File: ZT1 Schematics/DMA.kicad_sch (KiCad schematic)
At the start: 11 parts, among them U106 74LS32, U109 74LS368, U112 74LS368, U115 74LS32, U128 74LS74, U131 74LS08, U132 74LS10

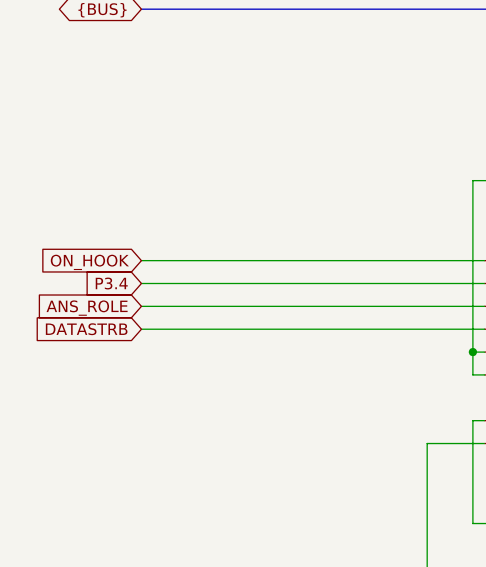
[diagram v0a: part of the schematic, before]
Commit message: Minor touchups
Fixed some of the text
Added some explanations
Simplified the video circuit
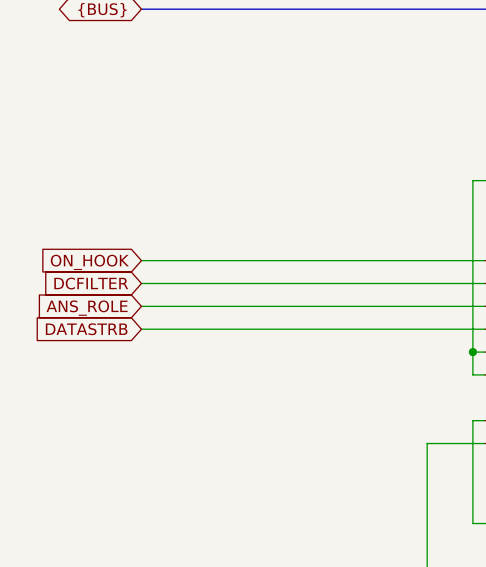
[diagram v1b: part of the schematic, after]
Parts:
- C115, C139: footprint ZX1:C_350mil -> ZT1:C_350mil
- R153: footprint ZX1:R_450mil -> ZT1:R_450mil
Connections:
- net P3.4 renamed DCFILTER
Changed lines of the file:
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@@
 		)
 	)
-	(global_label "P3.4"
+	(global_label "DCFILTER"
 		(shape input)
 		(at 43.18 93.98 180)
@@
 		)
 		(property "Intersheetrefs" "${INTERSHEET_REFS}"
-			(at 35.901 93.98 0)
+			(at 31.5467 93.98 0)
 			(effects
 				(font
@@
 		)
 		(instances
-			(project "ZX1"
+			(project "ZT1"
 				(path "/f4096561-d684-4672-ab54-4b1ef20fc4c8/ca6d4eac-07c0-4b7b-97f3-ce02b2439cee"
 					(reference "#PWR094")
@@
 	)
 	(symbol
-		(lib_name "74LS10_2")
 		(lib_id "74xx:74LS10")
 		(at 170.18 45.72 0)
@@
 		)
 		(instances
-			(project "ZX1"
+			(project "ZT1"
 				(path "/f4096561-d684-4672-ab54-4b1ef20fc4c8/ca6d4eac-07c0-4b7b-97f3-ce02b2439cee"
 					(reference "U132")
@@
 		)
 		(instances
-			(project "ZX1"
+			(project "ZT1"
 				(path "/f4096561-d684-4672-ab54-4b1ef20fc4c8/ca6d4eac-07c0-4b7b-97f3-ce02b2439cee"
 					(reference "U115")
@@
 		)
 		(instances
-			(project "ZX1"
+			(project "ZT1"
 				(path "/f4096561-d684-4672-ab54-4b1ef20fc4c8/ca6d4eac-07c0-4b7b-97f3-ce02b2439cee"
 					(reference "U112")
@@
 		)
 		(instances
-			(project "ZX1"
+			(project "ZT1"
 				(path "/f4096561-d684-4672-ab54-4b1ef20fc4c8/ca6d4eac-07c0-4b7b-97f3-ce02b2439cee"
 					(reference "#PWR093")
@@
 			)
 		)
-		(property "Footprint" "ZX1:C_350mil"
+		(property "Footprint" "ZT1:C_350mil"
 			(at 107.95 81.5848 0)
 			(effects
@@
 			)
 		)
-		(property "Datasheet" ""
+		(property "Datasheet" "~"
 			(at 104.14 82.55 0)
 			(effects
@@
 			)
 		)
-		(property "Description" ""
+		(property "Description" "Unpolarized capacitor"
 			(at 104.14 82.55 0)
 			(effects
@@
 		)
 		(instances
-			(project "ZX1"
+			(project "ZT1"
 				(path "/f4096561-d684-4672-ab54-4b1ef20fc4c8/ca6d4eac-07c0-4b7b-97f3-ce02b2439cee"
 					(reference "#PWR092")
@@
 		)
 		(instances
-			(project "ZX1"
+			(project "ZT1"
 				(path "/f4096561-d684-4672-ab54-4b1ef20fc4c8/ca6d4eac-07c0-4b7b-97f3-ce02b2439cee"
 					(reference "#PWR090")
@@
 			)
 		)
-		(property "Footprint" "ZX1:C_350mil"
+		(property "Footprint" "ZT1:C_350mil"
 			(at 262.89 29.5148 0)
 			(effects
@@
 			)
 		)
-		(property "Datasheet" ""
+		(property "Datasheet" "~"
 			(at 259.08 30.48 0)
 			(effects
@@
 			)
 		)
-		(property "Description" ""
+		(property "Description" "Unpolarized capacitor"
 			(at 259.08 30.48 0)
 			(effects
@@
 		)
 		(instances
-			(project "ZX1"
+			(project "ZT1"
 				(path "/f4096561-d684-4672-ab54-4b1ef20fc4c8/ca6d4eac-07c0-4b7b-97f3-ce02b2439cee"
 					(reference "U128")
@@
 		)
 		(instances
-			(project "ZX1"
+			(project "ZT1"
 				(path "/f4096561-d684-4672-ab54-4b1ef20fc4c8/ca6d4eac-07c0-4b7b-97f3-ce02b2439cee"
 					(reference "U128")
@@
 		)
 		(instances
-			(project "ZX1"
+			(project "ZT1"
 				(path "/f4096561-d684-4672-ab54-4b1ef20fc4c8/ca6d4eac-07c0-4b7b-97f3-ce02b2439cee"
 					(reference "U128")
@@
 			)
 		)
-		(property "Footprint" "ZX1:R_450mil"
+		(property "Footprint" "ZT1:R_450mil"
 			(at 118.618 35.56 90)
 			(effects
@@
 			)
 		)
-		(property "Datasheet" ""
+		(property "Datasheet" "~"
 			(at 116.84 35.56 0)
 			(effects
@@
 			)
 		)
-		(property "Description" ""
+		(property "Description" "Resistor"
 			(at 116.84 35.56 0)
 			(effects
@@
 		)
 		(instances
-			(project "ZX1"
+			(project "ZT1"
 				(path "/f4096561-d684-4672-ab54-4b1ef20fc4c8/ca6d4eac-07c0-4b7b-97f3-ce02b2439cee"
 					(reference "R153")
@@
 		)
 		(instances
-			(project "ZX1"
+			(project "ZT1"
 				(path "/f4096561-d684-4672-ab54-4b1ef20fc4c8/ca6d4eac-07c0-4b7b-97f3-ce02b2439cee"
 					(reference "U109")
@@
 		)
 		(instances
-			(project "ZX1"
+			(project "ZT1"
 				(path "/f4096561-d684-4672-ab54-4b1ef20fc4c8/ca6d4eac-07c0-4b7b-97f3-ce02b2439cee"
 					(reference "U106")
@@
 			)
 		)
-		(property "Datasheet" ""
+		(property "Datasheet" "~"
 			(at 269.24 93.98 0)
 			(effects
@@
 			)
 		)
-		(property "Description" ""
+		(property "Description" "Generic connector, single row, 01x16, script generated (kicad-library-utils/schlib/autogen/connector/)"
 			(at 269.24 93.98 0)
 			(effects
@@
 		)
 		(instances
-			(project "ZX1"
+			(project "ZT1"
 				(path "/f4096561-d684-4672-ab54-4b1ef20fc4c8/ca6d4eac-07c0-4b7b-97f3-ce02b2439cee"
 					(reference "S103")
@@
 		)
 		(instances
-			(project "ZX1"
+			(project "ZT1"
 				(path "/f4096561-d684-4672-ab54-4b1ef20fc4c8/ca6d4eac-07c0-4b7b-97f3-ce02b2439cee"
 					(reference "#PWR095")
@@
 		)
 		(instances
-			(project "ZX1"
+			(project "ZT1"
 				(path "/f4096561-d684-4672-ab54-4b1ef20fc4c8/ca6d4eac-07c0-4b7b-97f3-ce02b2439cee"
 					(reference "#PWR091")
@@
 		)
 		(instances
-			(project "ZX1"
+			(project "ZT1"
 				(path "/f4096561-d684-4672-ab54-4b1ef20fc4c8/ca6d4eac-07c0-4b7b-97f3-ce02b2439cee"
 					(reference "#PWR028")
@@
 		)
 		(instances
-			(project "ZX1"
+			(project "ZT1"
 				(path "/f4096561-d684-4672-ab54-4b1ef20fc4c8/ca6d4eac-07c0-4b7b-97f3-ce02b2439cee"
 					(reference "U131")
